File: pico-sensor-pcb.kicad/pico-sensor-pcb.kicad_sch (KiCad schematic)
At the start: 36 parts, among them J1 Conn_PDM, J10 Conn_PCB_2, J11 Conn_I2C1, J13 Conn_I2C1, J2 Conn_RUN_ON, J7 Conn_PCB_1, SW1 SW_Push, SW2 SW_Push, SW3 SW_Push, SW4 SW_Push, SW5 SW_Push, U1 AHT20, U2 BH1750FVI-TR, U3 SCD40_Breakout, U4 ENS160_Breakout

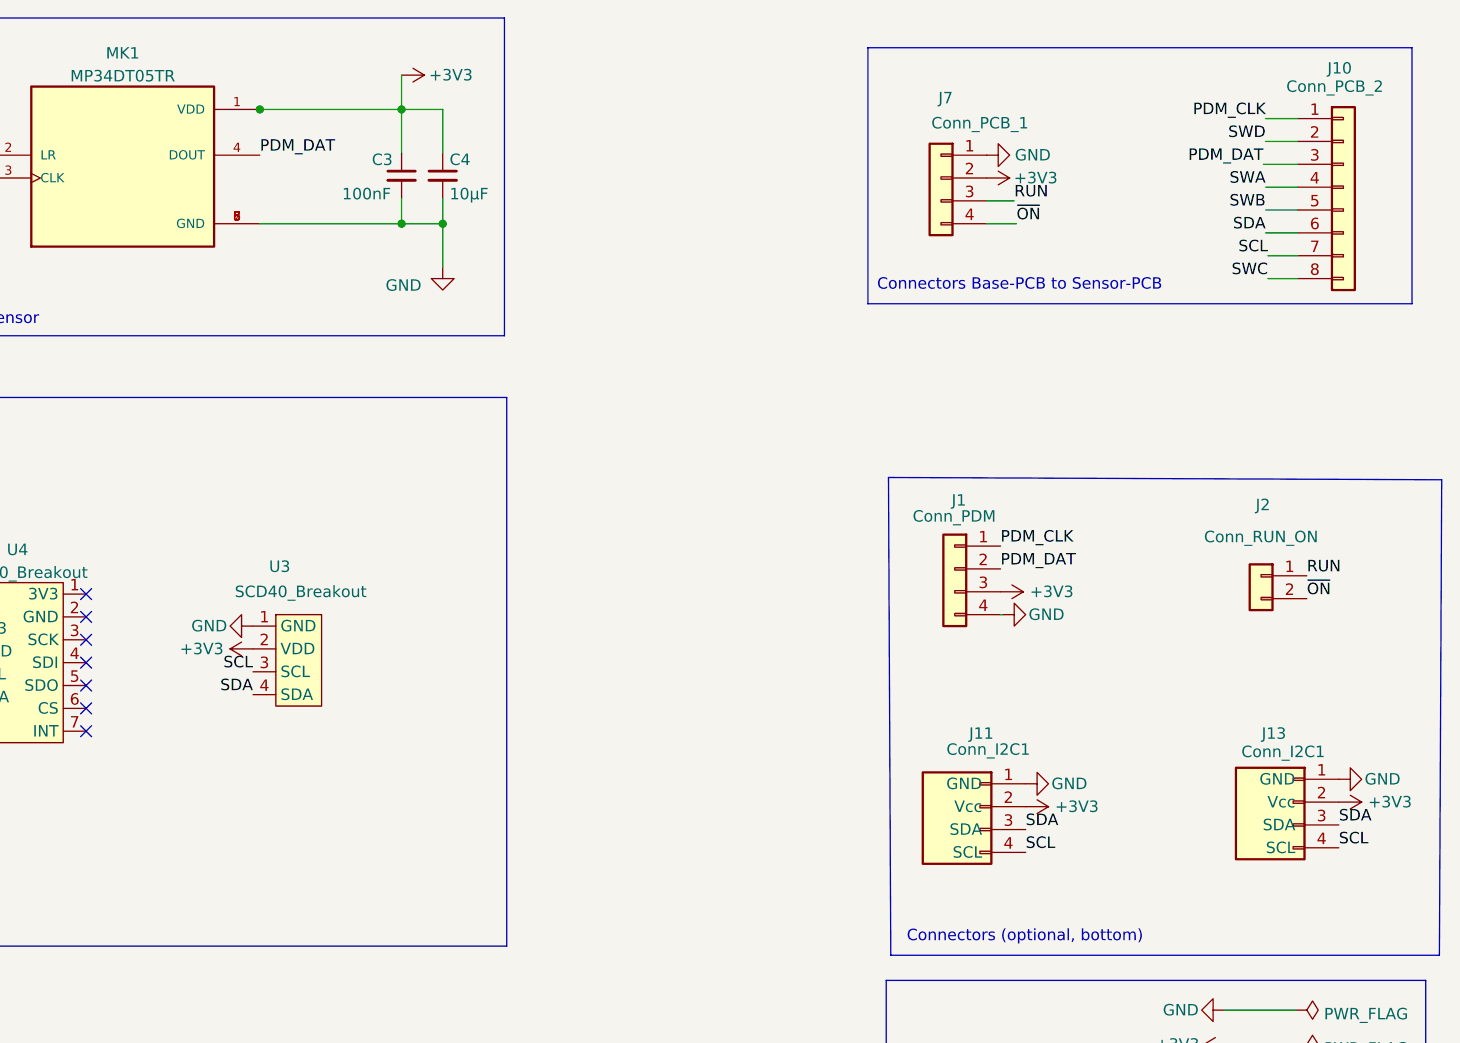
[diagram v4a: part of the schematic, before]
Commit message: add compatibility-connector for application-controls (A-D)
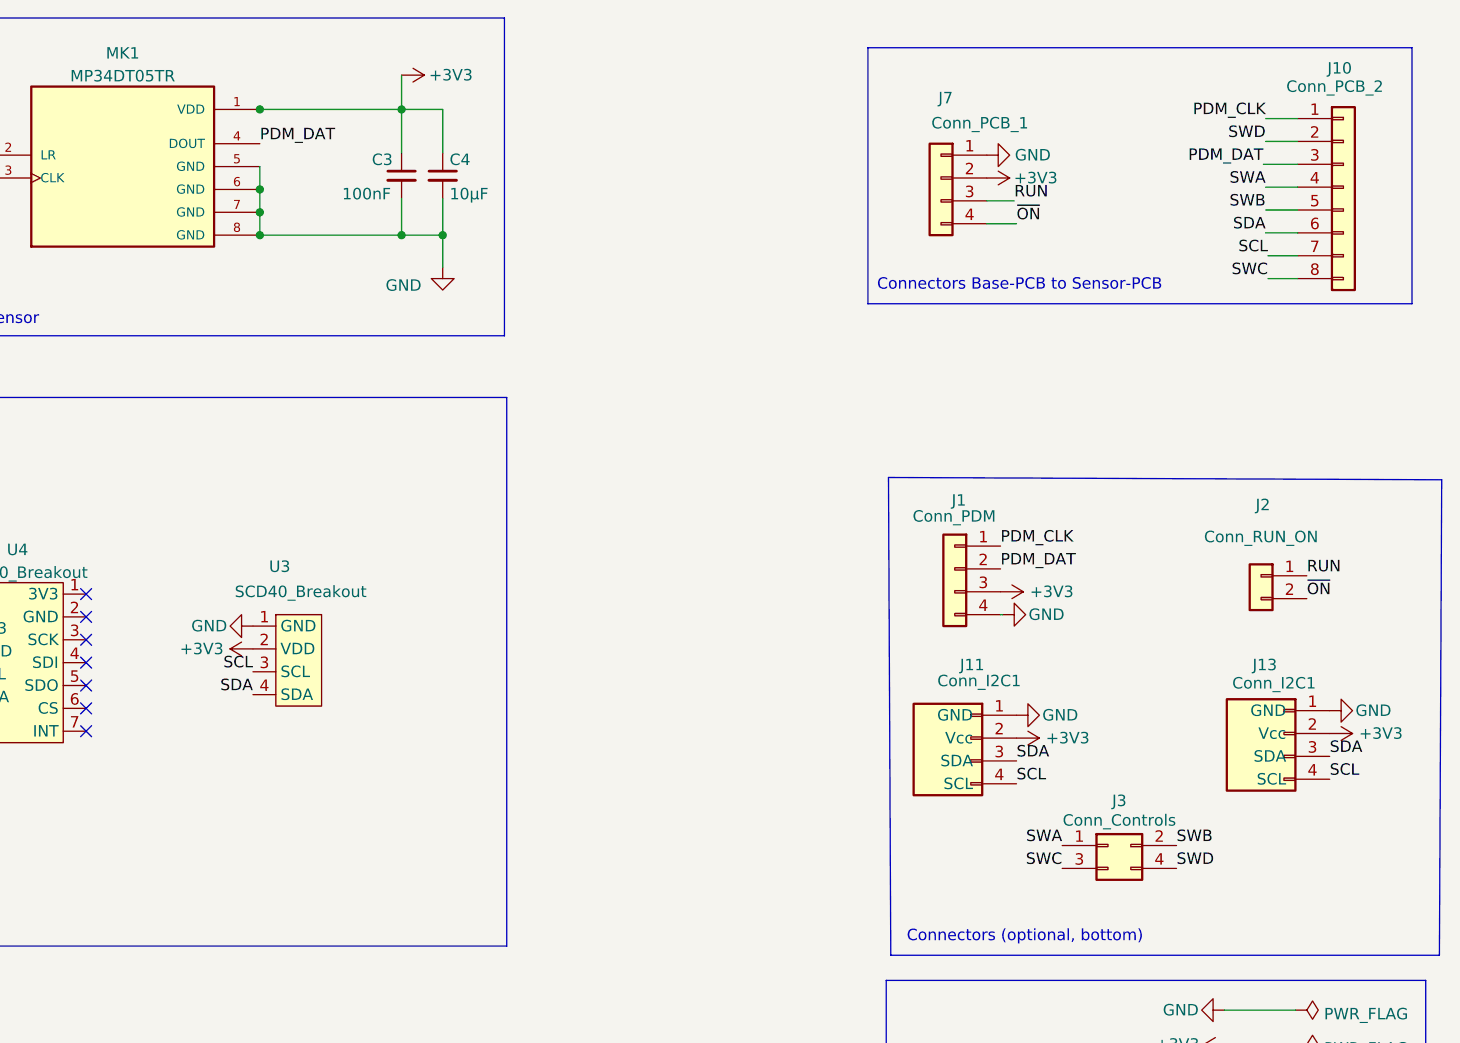
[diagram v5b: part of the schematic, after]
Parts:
- added J3: Conn_Controls, Connector_PinHeader_2.54mm:PinHeader_2x02_P2.54mm_Vertical, symbol Connector_Generic:Conn_02x02_Odd_Even
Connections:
- net SWA: now also J3.1 (Pin_1)
- net SWB: now also J3.2 (Pin_2)
- net SWC: now also J3.3 (Pin_3)
- net SWD: now also J3.4 (Pin_4)
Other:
- moved on the sheet: J11, J13

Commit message: Rev. 0.80: fixed PCB-connectors
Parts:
- J1, J2, J3, JP1, JP2, U3: now left out of the parts list
- MK1: LCSC (none) -> C2688664
- R1: LCSC C22962 -> C25091
- U1: LCSC (none) -> C3012622
- U2: LCSC (none) -> C78960
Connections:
- net +3V3: now also J7.3 (Pin_3); no longer J7.2 (Pin_2)
- net GND: now also J7.4 (Pin_4); no longer J7.1 (Pin_1)
- net PDM_CLK: now also J10.8 (Pin_8); no longer J10.1 (Pin_1)
- net PDM_DAT: now also J10.6 (Pin_6); no longer J10.3 (Pin_3)
- net RUN: now also J7.2 (Pin_2); no longer J7.3 (Pin_3)
- net SCL: now also J10.2 (Pin_2); no longer J10.7 (Pin_7)
- net SDA: now also J10.3 (Pin_3); no longer J10.6 (Pin_6)
- net SWA: now also J10.5 (Pin_5); no longer J10.4 (Pin_4)
- net SWB: now also J10.4 (Pin_4); no longer J10.5 (Pin_5)
- net SWC: now also J10.1 (Pin_1); no longer J10.8 (Pin_8)
- net SWD: now also J10.7 (Pin_7); no longer J10.2 (Pin_2)
- net ~{ON}: now also J7.1 (Pin_1); no longer J7.4 (Pin_4)
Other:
- moved on the sheet: J7
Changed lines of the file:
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@@
   (title_block
     (title "pico-sensor-pcb")
-    (date "2023-10-07")
-    (rev "0.71")
+    (date "2023-10-14")
+    (rev "0.80")
     (company "Bernhard Bablok")
     (comment 1 "https://github.com/bablokb/pcb-pico-datalogger")
@@
   )
   (symbol (lib_id "Jumper:Jumper_2_Open") (at 37.846 101.6 270) (unit 1)
-    (in_bom yes) (on_board yes)
+    (in_bom no) (on_board yes)
     (property "Reference" "JP1" (id 0) (at 32.258 100.838 90)
       (effects (font (size 1.27 1.27)) (justify left))
@@
       (effects (font (size 1.27 1.27)) hide)
     )
+    (property "LCSC" "C2688664" (id 4) (at 134.366 39.37 0)
+      (effects (font (size 1.27 1.27)) hide)
+    )
     (pin "1")
     (pin "2")
@@
       (effects (font (size 1.27 1.27)) (justify bottom) hide)
     )
+    (property "LCSC" "C3012622" (id 13) (at 45.212 38.608 0)
+      (effects (font (size 1.27 1.27)) hide)
+    )
     (pin "1")
     (pin "2")
@@
   )
   (symbol (lib_id "Jumper:Jumper_2_Open") (at 238.506 153.162 0) (unit 1)
-    (in_bom yes) (on_board yes) (fields_autoplaced)
+    (in_bom no) (on_board yes) (fields_autoplaced)
     (property "Reference" "JP2" (id 0) (at 238.506 147.8112 0))
     (property "Value" "JP_Power" (id 1) (at 238.506 150.3481 0))
@@
   )
   (symbol (lib_id "Connector_Generic:Conn_02x02_Odd_Even") (at 243.84 116.078 0) (unit 1)
-    (in_bom yes) (on_board yes)
+    (in_bom no) (on_board yes)
     (property "Reference" "J3" (id 0) (at 245.11 111.1082 0))
     (property "Value" "Conn_Controls" (id 1) (at 245.11 113.284 0))
@@
     (pin "2")
   )
-  (symbol (lib_id "Connector_Generic:Conn_01x04") (at 225.298 41.91 0) (mirror y) (unit 1)
-    (in_bom yes) (on_board yes)
-    (property "Reference" "J7" (id 0) (at 225.806 33.02 0))
-    (property "Value" "Conn_PCB_1" (id 1) (at 229.616 35.814 0))
-    (property "Footprint" "Connector_JST:JST_SUR_BM04B-SURS-TF_1x04-1MP_P0.80mm_Vertical" (id 2) (at 225.298 41.91 0)
-      (effects (font (size 1.27 1.27)) hide)
-    )
-    (property "Datasheet" "~" (id 3) (at 225.298 41.91 0)
-      (effects (font (size 1.27 1.27)) hide)
-    )
-    (property "LCSC" "C495551 " (id 4) (at 225.298 41.91 0)
+  (symbol (lib_id "Connector_Generic:Conn_01x04") (at 225.298 44.45 180) (unit 1)
+    (in_bom yes) (on_board yes)
+    (property "Reference" "J7" (id 0) (at 225.044 35.306 0))
+    (property "Value" "Conn_PCB_1" (id 1) (at 227.076 32.004 0))
+    (property "Footprint" "Connector_JST:JST_SUR_BM04B-SURS-TF_1x04-1MP_P0.80mm_Vertical" (id 2) (at 225.298 44.45 0)
+      (effects (font (size 1.27 1.27)) hide)
+    )
+    (property "Datasheet" "~" (id 3) (at 225.298 44.45 0)
+      (effects (font (size 1.27 1.27)) hide)
+    )
+    (property "LCSC" "C495551 " (id 4) (at 225.298 44.45 0)
       (effects (font (size 1.27 1.27)) hide)
     )
@@
   )
   (symbol (lib_id "user:SCD40_Breakout") (at 153.924 94.234 0) (unit 1)
-    (in_bom yes) (on_board yes)
+    (in_bom no) (on_board yes)
     (property "Reference" "U3" (id 0) (at 150.622 85.09 0)
       (effects (font (size 1.27 1.27)) (justify left))
@@
   )
   (symbol (lib_id "Connector_Generic:Conn_01x02") (at 260.858 86.106 0) (mirror y) (unit 1)
-    (in_bom yes) (on_board yes)
+    (in_bom no) (on_board yes)
     (property "Reference" "J2" (id 0) (at 261.874 78.232 0)
       (effects (font (size 1.27 1.27)) (justify left))
@@
       (effects (font (size 1.27 1.27)) hide)
     )
-    (property "LCSC" "C22962" (id 4) (at 73.914 28.702 0)
-      (effects (font (size 1.27 1.27)) hide)
-    )
-    (pin "1")
-    (pin "2")
-  )
-  (symbol (lib_id "Connector_Generic:Conn_01x08") (at 270.002 42.926 0) (unit 1)
-    (in_bom yes) (on_board yes)
-    (property "Reference" "J10" (id 0) (at 268.224 29.718 0)
-      (effects (font (size 1.27 1.27)) (justify left))
-    )
-    (property "Value" "Conn_PCB_2" (id 1) (at 263.652 31.75 0)
-      (effects (font (size 1.27 1.27)) (justify left))
-    )
-    (property "Footprint" "Connector_JST:JST_SUR_BM08B-SURS-TF_1x08-1MP_P0.80mm_Vertical" (id 2) (at 270.002 42.926 0)
-      (effects (font (size 1.27 1.27)) hide)
-    )
-    (property "Datasheet" "~" (id 3) (at 270.002 42.926 0)
-      (effects (font (size 1.27 1.27)) hide)
-    )
-    (property "LCSC" "C5143489" (id 4) (at 270.002 42.926 0)
+    (property "LCSC" "C25091" (id 4) (at 73.914 28.702 0)
+      (effects (font (size 1.27 1.27)) hide)
+    )
+    (pin "1")
+    (pin "2")
+  )
+  (symbol (lib_id "Connector_Generic:Conn_01x08") (at 270.002 45.466 0) (mirror x) (unit 1)
+    (in_bom yes) (on_board yes)
+    (property "Reference" "J10" (id 0) (at 267.97 32.258 0)
+      (effects (font (size 1.27 1.27)) (justify left))
+    )
+    (property "Value" "Conn_PCB_2" (id 1) (at 261.62 29.718 0)
+      (effects (font (size 1.27 1.27)) (justify left))
+    )
+    (property "Footprint" "Connector_JST:JST_SUR_BM08B-SURS-TF_1x08-1MP_P0.80mm_Vertical" (id 2) (at 270.002 45.466 0)
+      (effects (font (size 1.27 1.27)) hide)
+    )
+    (property "Datasheet" "~" (id 3) (at 270.002 45.466 0)
+      (effects (font (size 1.27 1.27)) hide)
+    )
+    (property "LCSC" "C5143489" (id 4) (at 270.002 45.466 0)
       (effects (font (size 1.27 1.27)) hide)
     )
@@
       (effects (font (size 1.27 1.27)) hide)
     )
+    (property "LCSC" "C78960" (id 4) (at 57.658 88.138 0)
+      (effects (font (size 1.27 1.27)) hide)
+    )
     (pin "1")
     (pin "2")
@@
   )
   (symbol (lib_id "Connector_Generic:Conn_01x04") (at 226.822 85.344 0) (mirror y) (unit 1)
-    (in_bom yes) (on_board yes)
+    (in_bom no) (on_board yes)
     (property "Reference" "J1" (id 0) (at 228.092 77.724 0)
       (effects (font (size 1.27 1.27)) (justify left))

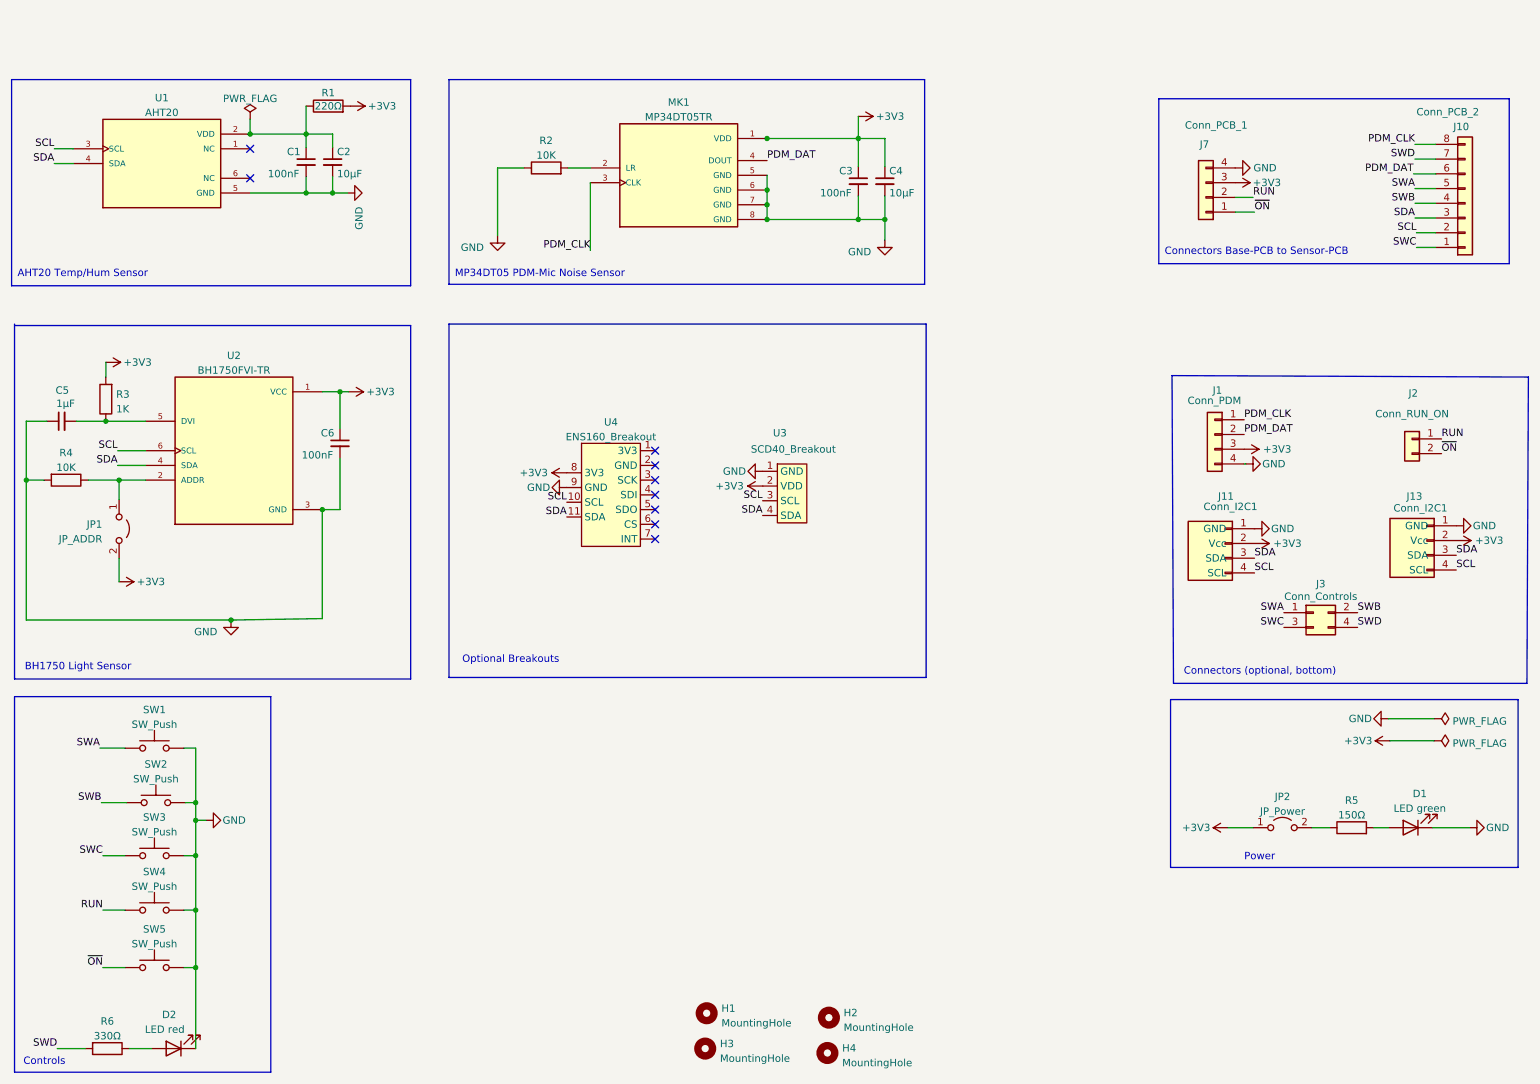
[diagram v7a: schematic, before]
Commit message: Sensor-PCB Rev 1.95: larger PCB, I2C-pullups, labels (ready for review)
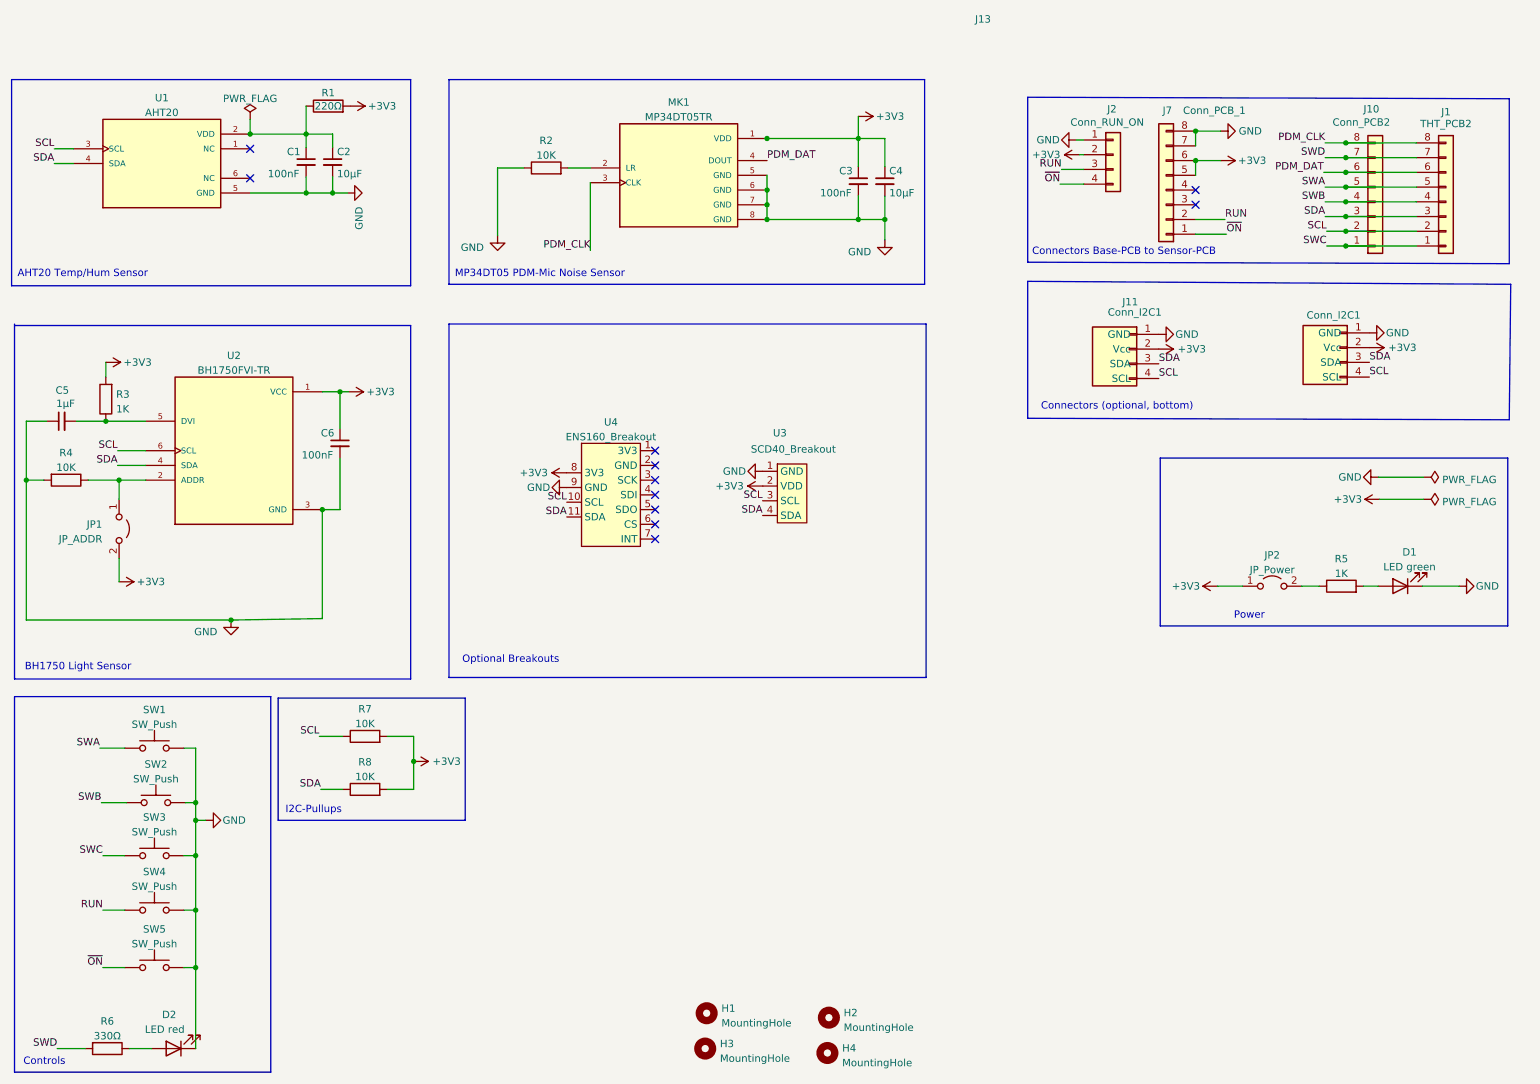
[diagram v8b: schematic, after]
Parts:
- removed J1: Conn_PDM, Connector_PinHeader_2.54mm:PinHeader_1x04_P2.54mm_Vertical, symbol Connector_Generic:Conn_01x04
- removed J3: Conn_Controls, Connector_PinHeader_2.54mm:PinHeader_2x02_P2.54mm_Vertical, symbol Connector_Generic:Conn_02x02_Odd_Even
- removed J7: Conn_PCB_1, Connector_JST:JST_SUR_BM04B-SURS-TF_1x04-1MP_P0.80mm_Vertical, symbol Connector_Generic:Conn_01x04
- added J1: THT_PCB2, Connector_PinHeader_2.54mm:PinHeader_1x08_P2.54mm_Vertical, symbol Connector_Generic:Conn_01x08
- added J7: Conn_PCB_1, Connector_JST:JST_SUR_BM08B-SURS-TF_1x08-1MP_P0.80mm_Vertical, symbol Connector_Generic:Conn_01x08
- added R7, R8: 10K, Resistor_SMD:R_0402_1005Metric, symbol Device:R
- J10: value Conn_PCB_2 -> Conn_PCB2
- J2: footprint Connector_PinHeader_2.54mm:PinHeader_1x02_P2.54mm_Vertical -> Connector_PinHeader_2.54mm:PinHeader_1x04_P2.54mm_Vertical; symbol Connector_Generic:Conn_01x02 -> Connector_Generic:Conn_01x04
- R5: value 150Ω -> 1K; LCSC C25082 -> C11702
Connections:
- net +3V3: now also J2.2 (Pin_2), J7.5 (Pin_5), J7.6 (Pin_6), R7.2, R8.2
- net GND: now also J2.1 (Pin_1), J7.7 (Pin_7), J7.8 (Pin_8)
- net PDM_CLK: now also J1.8 (Pin_8)
- net PDM_DAT: now also J1.6 (Pin_6)
- net RUN: now also J2.3 (Pin_3), J7.2 (Pin_2); no longer J2.1 (Pin_1)
- net SCL: now also J1.2 (Pin_2), R7.1
- net SDA: now also J1.3 (Pin_3), R8.1
- net SWA: now also J1.5 (Pin_5)
- net SWB: now also J1.4 (Pin_4)
- net SWC: now also J1.1 (Pin_1)
- net SWD: now also J1.7 (Pin_7)
- net ~{ON}: now also J2.4 (Pin_4), J7.1 (Pin_1); no longer J2.2 (Pin_2)
- no-connect marks 9 -> 11
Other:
- note added: "I2C-Pullups"
- moved on the sheet: D1, J10, J11, J13, JP2, R5
